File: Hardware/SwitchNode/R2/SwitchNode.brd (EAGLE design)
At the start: 67.1 x 45.7 mm, 28 parts, among them T1 2SC1815, T2 2SC1815, T3 C1815

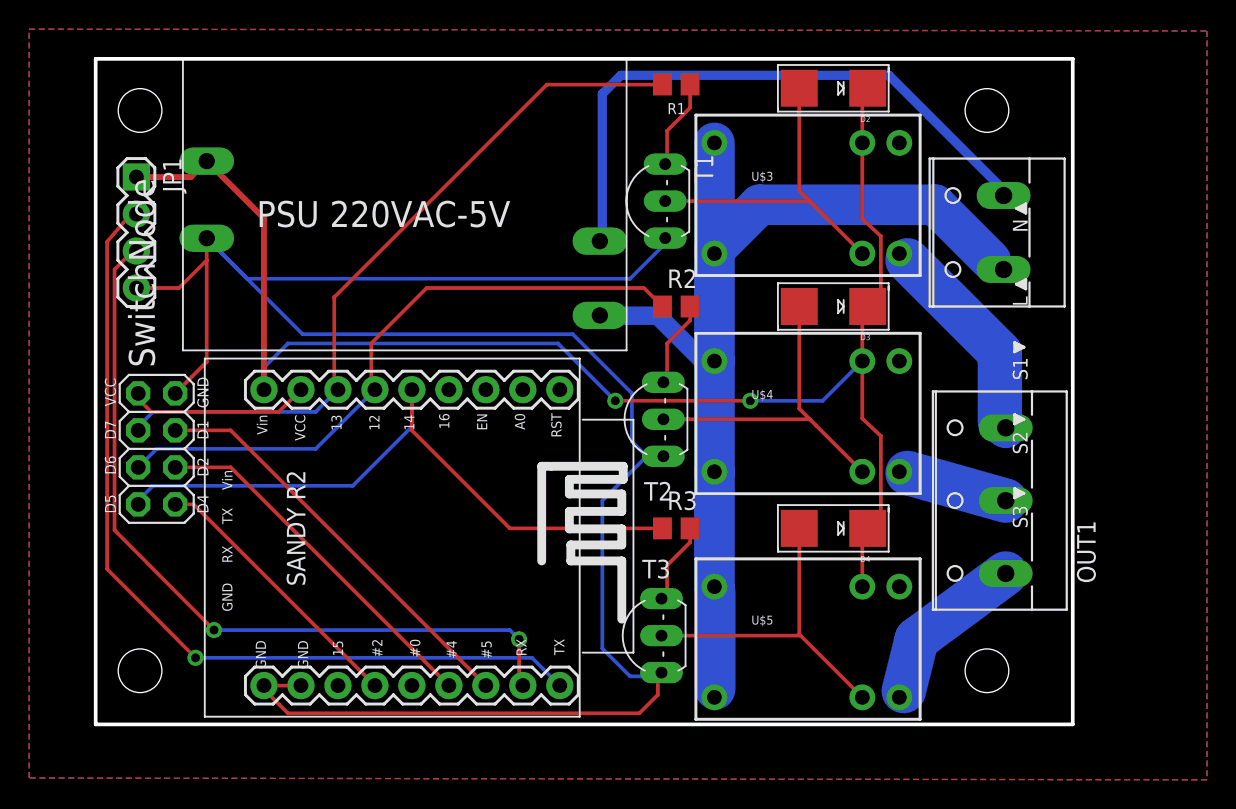
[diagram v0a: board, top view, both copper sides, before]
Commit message: Correct PSU pinouts and update labels for SwitchNode R2
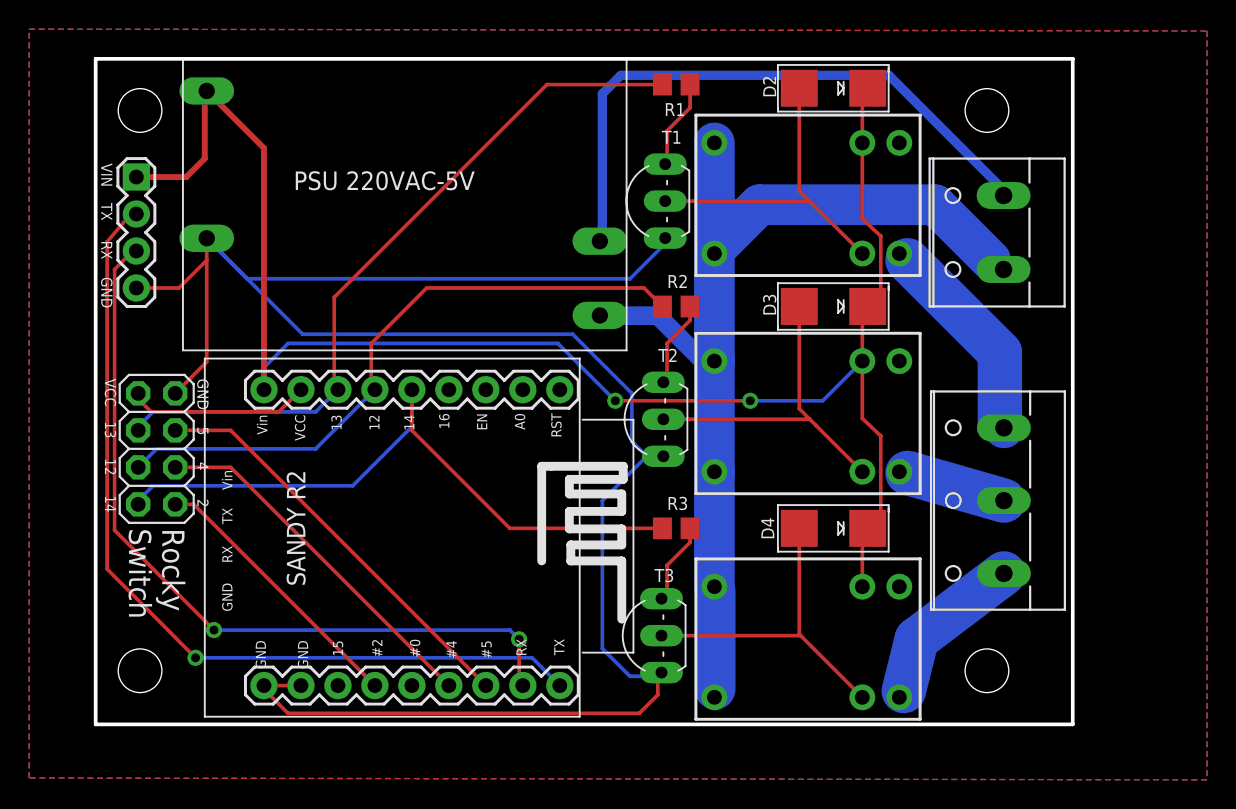
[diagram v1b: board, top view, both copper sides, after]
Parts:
- removed U$10: (no value), dicons:ICON_EXL-S
- added U$17: (no value), dicons:ICON_EXL-S
- moved U$14 4.46 mm to (91.7, 50.4), flipped to the bottom, turned to 0 degrees
- moved U$13 4.32 mm to (91.7, 55.5), flipped to the bottom, turned to 0 degrees
- moved U$15 3.77 mm to (91.7, 46.1), flipped to the bottom, turned to 0 degrees
- moved U$12 2.40 mm to (90.7, 65.8), flipped to the bottom, turned to 180 degrees
- moved U$11 2.29 mm to (90.7, 70.9), flipped to the bottom, turned to 180 degrees
- moved OUT1 0.13 mm to (87.2, 48.9)
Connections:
- removed net D0: U$2.D0
- removed net D1: JP2.4, U$2.D1
- removed net D2: JP2.6, U$2.D2
- removed net D3: U$2.D3
- removed net D4: JP2.8, U$2.D4
- removed net D5: JP2.7, R3.1, U$2.D5
- removed net D6: JP2.5, R2.1, U$2.D6
- removed net D7: JP2.3, R1.1, U$2.D7
- new net 0: U$2.0
- new net 12: JP2.5, R2.1, U$2.12
- new net 13: JP2.3, R1.1, U$2.13
- new net 14: JP2.7, R3.1, U$2.14
- new net 16: U$2.16
- new net 2: JP2.8, U$2.2
- new net 4: JP2.6, U$2.4
- new net 5: JP2.4, U$2.5
- net D8: now also U$2.15; no longer U$2.D8
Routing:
- net D7: track 50.1 -> 0.00 mm
- net 13: track 0.00 -> 50.1 mm
- net D5: track 46.5 -> 0.00 mm
- net 14: track 0.00 -> 46.5 mm
- net D6: track 43.9 -> 0.00 mm
- net 12: track 0.00 -> 43.9 mm
- net D1: track 28.6 -> 0.00 mm
- net 5: track 0.00 -> 28.6 mm
- net D2: track 25.0 -> 0.00 mm
- net 4: track 0.00 -> 25.0 mm
- net D4: track 18.9 -> 0.00 mm
- net 2: track 0.00 -> 18.9 mm
- net 5V: track 105.3 -> 114.7 mm
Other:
- board text added: "12"
- board text added: "13"
- board text added: "14"
- board text added: "2"
- board text added: "4"
- board text added: "5"
- board text added: "HIGH VOLTAGE"
- board text added: "RX"
- board text added: "Rocky Switch"
- board text added: "TX"
- board text added: "VIN"
- board text removed: "**HIGH VOLTAGE**"
- board text removed: "D1"
- board text removed: "D2"
- board text removed: "D4"
- board text removed: "D5"
- board text removed: "D6"
- board text removed: "D7"
- board text removed: "SwitchNode"
